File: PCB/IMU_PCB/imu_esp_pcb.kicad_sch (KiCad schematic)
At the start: 25 parts, among them J1 Conn_01x02_Pin, J2 Conn_01x05_Pin, U1 MPU-6050, U2 ESP32-C3-WROOM-02, U3 PTS647SM38SMTR2LFS, U4 XC6206P332MR-G, U5 1N5819HW-7-F

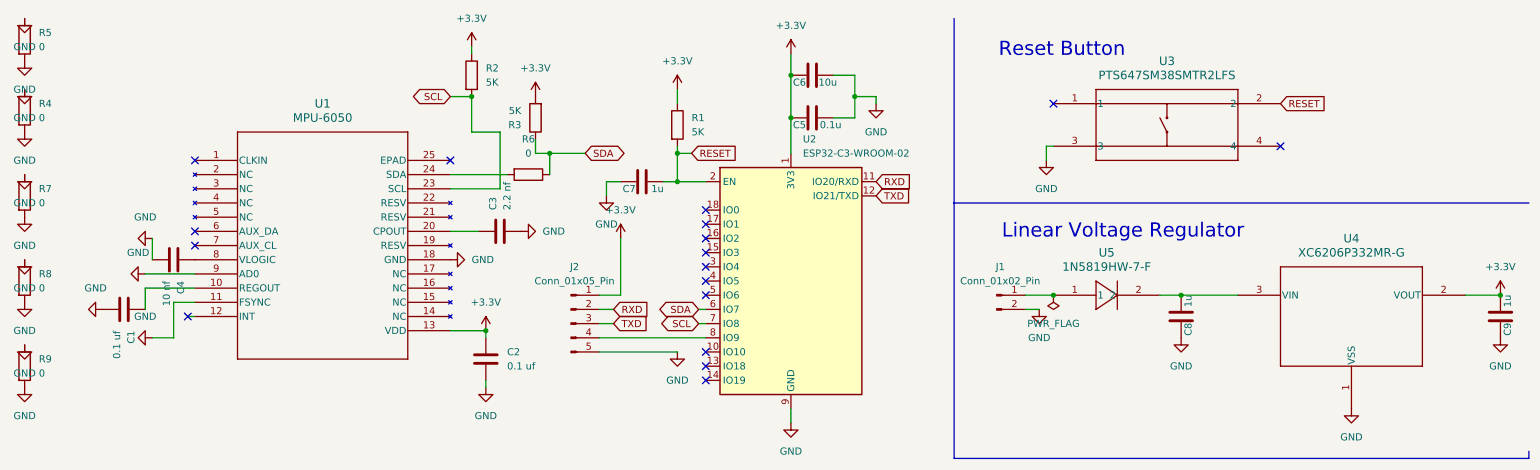
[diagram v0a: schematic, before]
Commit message: New IMU Schematic with BMI270
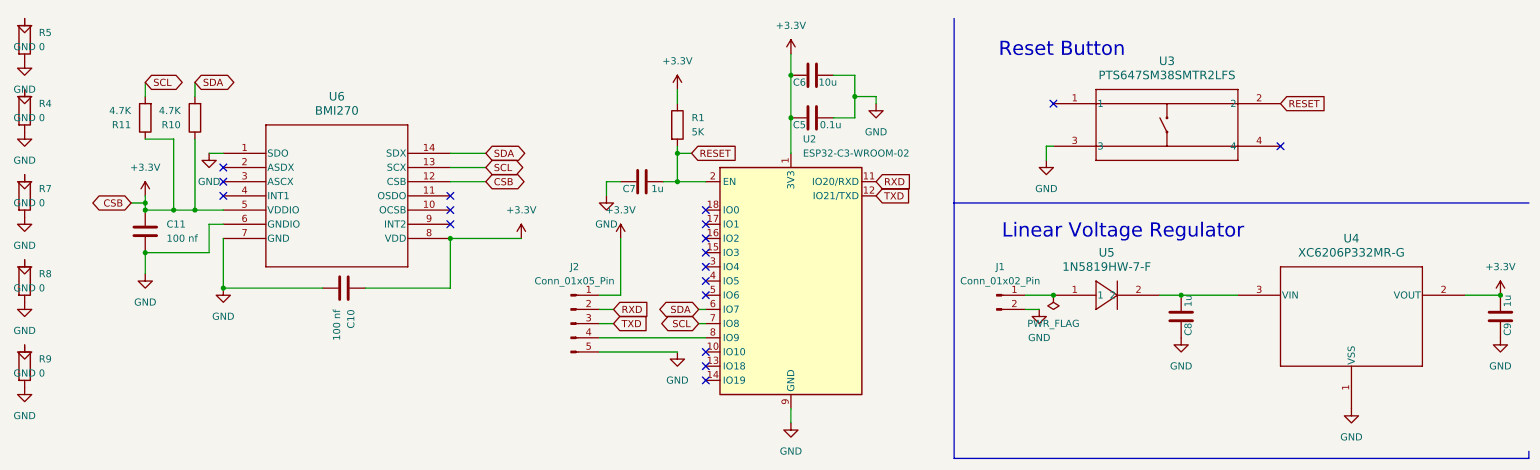
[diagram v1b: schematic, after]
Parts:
- removed C1, C2: 0.1 uf, Capacitor_SMD:C_0805_2012Metric_Pad1.18x1.45mm_HandSolder, symbol Device:C
- removed C3: 2.2 nf, Capacitor_SMD:C_0805_2012Metric_Pad1.18x1.45mm_HandSolder, symbol Device:C
- removed C4: 10 nf, Capacitor_SMD:C_0805_2012Metric_Pad1.18x1.45mm_HandSolder, symbol Device:C
- removed R2, R3: 5K, Resistor_SMD:R_0805_2012Metric_Pad1.20x1.40mm_HandSolder, symbol Device:R
- removed R6: 0, Resistor_SMD:R_0805_2012Metric_Pad1.20x1.40mm_HandSolder, symbol Device:R
- removed U1: MPU-6050, footprints:QFN24_4X4X0P9-0P5_TDK, symbol 2026-01-30_16-01-32:MPU-6050
- added C10, C11: 100 nf, Capacitor_SMD:C_0805_2012Metric_Pad1.18x1.45mm_HandSolder, symbol Device:C
- added R10, R11: 4.7K, Resistor_SMD:R_0805_2012Metric_Pad1.20x1.40mm_HandSolder, symbol Device:R
- added U6: BMI270, BMI270_BOS, symbol 2026-03-06_17-42-29:BMI270
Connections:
- net +3.3V: now also C10.1, C11.1, R10.1, R11.1, U6.12 (CSB), U6.5 (VDDIO), U6.8 (VDD)
- net GND: now also C10.2, C11.2, U6.1 (SDO), U6.6 (GNDIO), U6.7 (GND)
- net SCL: now also R11.2, U6.13 (SCX)
- net SDA: now also R10.2, U6.14 (SDX)
- no-connect marks 17 -> 18

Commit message: PCB for IMU
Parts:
- removed R8, R9: 0, Resistor_SMD:R_0805_2012Metric_Pad1.20x1.40mm_HandSolder, symbol Device:R

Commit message: IMU PCB updated
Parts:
- removed R4, R5, R7: 0, Resistor_SMD:R_0805_2012Metric_Pad1.20x1.40mm_HandSolder, symbol Device:R

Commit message: Finalized Updated IMU PCB
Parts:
- removed C6: 10u, Capacitor_SMD:C_0805_2012Metric_Pad1.18x1.45mm_HandSolder, symbol Device:C
- added C1: UCS2G100MPD1TD, U1-T_NCH, symbol AluCap:UCS2G100MPD1TD
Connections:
- net +3.3V: now also C1.1
- net GND: now also C1.2
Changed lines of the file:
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@@
+	)
+	(junction
+		(at 199.39 62.23)
+		(diameter 0)
+		(color 0 0 0 0)
+	)
+	(junction
+		(at 41.91 46.99)
+		(diameter 0)
+		(color 0 0 0 0)
+	)
+	(junction
+		(at 163.83 26.67)
+		(diameter 0)
+		(color 0 0 0 0)
+	)
+	(junction
+		(at 132.08 36.83)
+		(diameter 0)
+		(color 0 0 0 0)
+	)
+	(junction
+		(at 45.72 46.99)
+		(diameter 0)
+		(color 0 0 0 0)
+	)
+	(junction
+		(at 36.83 46.99)
+		(diameter 0)
+		(color 0 0 0 0)
 	)
 	(junction
@@
 		(color 0 0 0 0)
 	)
-	(junction
-		(at 199.39 62.23)
-		(diameter 0)
-		(color 0 0 0 0)
-	)
-	(junction
-		(at 41.91 46.99)
-		(diameter 0)
-		(color 0 0 0 0)
-	)
-	(junction
-		(at 163.83 26.67)
-		(diameter 0)
-		(color 0 0 0 0)
-	)
-	(junction
-		(at 132.08 36.83)
-		(diameter 0)
-		(color 0 0 0 0)
-	)
-	(junction
-		(at 45.72 46.99)
-		(diameter 0)
-		(color 0 0 0 0)
-	)
-	(junction
-		(at 36.83 46.99)
-		(diameter 0)
-		(color 0 0 0 0)
-	)
 	(no_connect
 		(at 91.44 44.45)
@@
 	(wire
 		(pts
+			(xy 152.4 22.86) (xy 152.4 30.48)
+		)
+		(stroke
+			(width 0)
+			(type default)
+		)
+	)
+	(wire
+		(pts
 			(xy 36.83 24.13) (xy 36.83 26.67)
 		)
@@
 	(wire
 		(pts
-			(xy 152.4 22.86) (xy 152.4 30.48)
+			(xy 152.4 19.05) (xy 152.4 22.86)
 		)
 		(stroke
@@
 		(pts
 			(xy 284.48 45.72) (xy 181.61 45.72)
-		)
-		(stroke
-			(width 0)
-			(type default)
-		)
-	)
-	(wire
-		(pts
-			(xy 152.4 19.05) (xy 152.4 22.86)
 		)
 		(stroke
@@
 	)
 	(symbol
-		(lib_id "Device:C")
-		(at 156.21 22.86 90)
-		(unit 1)
-		(exclude_from_sim no)
-		(in_bom yes)
-		(on_board yes)
-		(dnp no)
-		(property "Reference" "C6"
-			(at 153.924 24.13 90)
-			(effects
-				(font
-					(size 1.27 1.27)
-				)
-			)
-		)
-		(property "Value" "10u"
-			(at 159.004 24.13 90)
-			(effects
-				(font
-					(size 1.27 1.27)
-				)
-			)
-		)
-		(property "Footprint" "Capacitor_SMD:C_0805_2012Metric_Pad1.18x1.45mm_HandSolder"
-			(at 160.02 21.8948 0)
-			(effects
-				(font
-					(size 1.27 1.27)
-				)
-				(hide yes)
-			)
-		)
-		(property "Datasheet" "~"
-			(at 156.21 22.86 0)
-			(effects
-				(font
-					(size 1.27 1.27)
-				)
-				(hide yes)
-			)
-		)
-		(property "Description" "Unpolarized capacitor"
-			(at 156.21 22.86 0)
-			(effects
-				(font
-					(size 1.27 1.27)
-				)
-				(hide yes)
-			)
-		)
-		(pin "1"
-		)
-		(pin "2"
-		)
-		(instances
-			(project ""
-				(path "/32e5ba35-9648-47f9-9581-dda55d5c3e51"
-					(reference "C6")
-					(unit 1)
-				)
-			)
-		)
-	)
-	(symbol
 		(lib_id "power:GND")
 		(at 152.4 85.09 0)
@@
 					(unit 1)
 				)
+			)
+		)
+	)
+	(symbol
+		(lib_id "AluCap:UCS2G100MPD1TD")
+		(at 152.4 22.86 0)
+		(unit 1)
+		(exclude_from_sim no)
+		(in_bom yes)
+		(on_board yes)
+		(dnp no)
+		(fields_autoplaced yes)
+		(property "Reference" "C1"
+			(at 156.21 16.51 0)
+			(effects
+				(font
+					(size 1.524 1.524)
+				)
+			)
+		)
+		(property "Value" "UCS2G100MPD1TD"
+			(at 156.21 19.05 0)
+			(effects
+				(font
+					(size 1.524 1.524)
+				)
+			)
+		)
+		(property "Footprint" "U1-T_NCH"
+			(at 152.4 22.86 0)
+			(effects
+				(font
+					(size 1.27 1.27)
+					(italic yes)
+				)
+				(hide yes)
+			)
+		)
+		(property "Datasheet" "UCS2G100MPD1TD"
+			(at 152.4 22.86 0)
+			(effects
+				(font
+					(size 1.27 1.27)
+					(italic yes)
+				)
+				(hide yes)
+			)
+		)
+		(property "Description" ""
+			(at 152.4 22.86 0)
+			(effects
+				(font
+					(size 1.27 1.27)
+				)
+				(hide yes)
+			)
+		)
+		(pin "1"
+		)
+		(pin "2"
+		)
+		(instances
+			(project ""
+				(path "/32e5ba35-9648-47f9-9581-dda55d5c3e51"
+					(reference "C1")
+					(unit 1)
+				)
